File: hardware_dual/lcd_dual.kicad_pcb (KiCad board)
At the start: 2 copper layers, 80 x 50 mm, 128 parts, among them J1 HDMI-A receptacle, J2 USB-C (power + touch USB), J3 AT070TN92 FPC (0.5mm 50P, top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, J4 Touch FPC 6P 0.5mm, J5 SWD/UART, Q1 AO3401A, Q2 2N7002, SW1 BOOT (DFU), SW2 BOOT CH32, U1 LT8619C, U10 STM32F072CBT6 / CH32X035C8T6, U2 AMS1117-3.3, U3 AMS1117-1.8, U4 USBLC6-2SC6, U7 TPS61040, U8 LM321, U9 TPS61165, Y1 25MHz 12pF

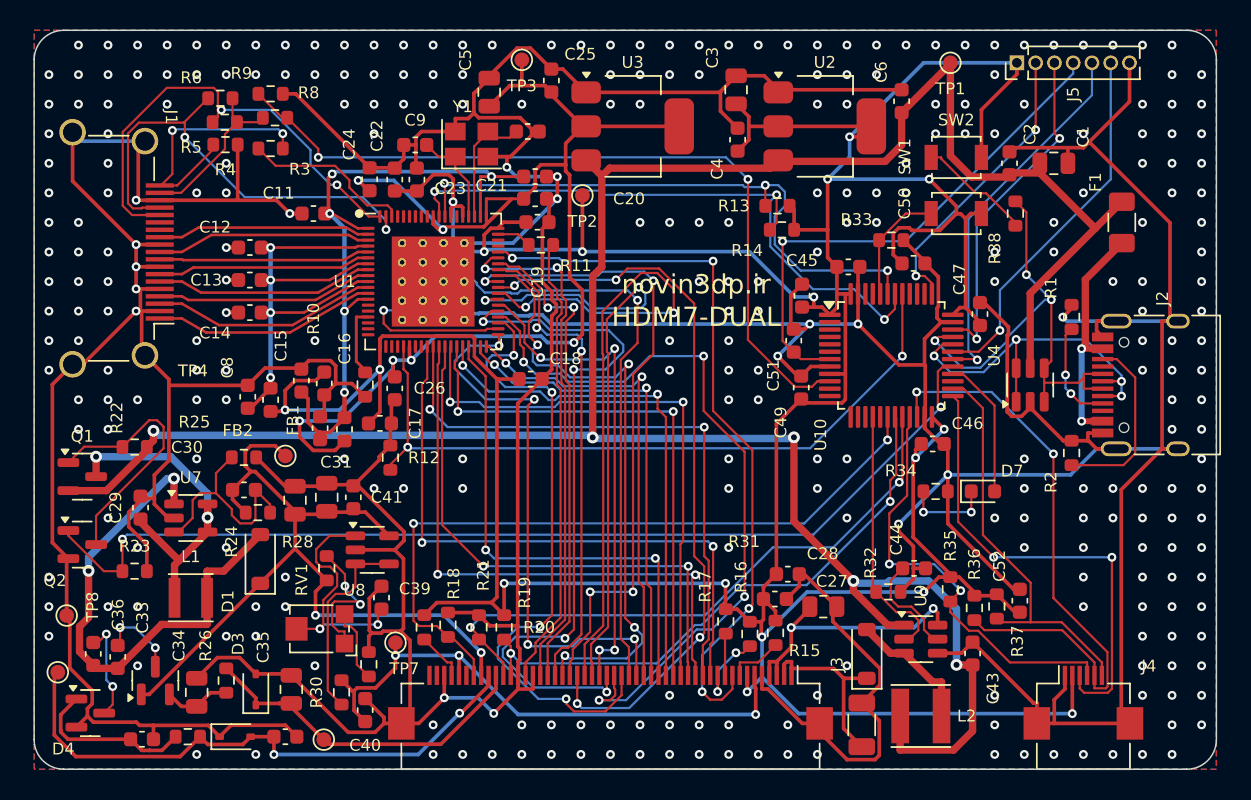
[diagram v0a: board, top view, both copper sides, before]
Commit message: Dual board: aligned passives; firmware: CH32X035 port
PCB (hardware_dual):
- Add a tidy pass after legalize: nearby resistors and capacitors are
  lined up in rows and columns, set to the same orientation and
  snapped to a 0.25 mm grid. A move is kept only if the courtyard
  stays clear (39 parts aligned).
- Rerouted: DRC 0 errors, 0 unconnected, netlist matches design.py.

Firmware:
- Chip-specific code (clock, GPIO, PWM, UART, flash, I2C, USB IRQ)
  now lives behind a small board HAL in src/stm32/ and src/ch32/.
  LT8619C, GT915, USB HID, panel, console and settings logic are
  shared. Both STM32 builds compile without warnings, at the same
  sizes as before.
- New target make BOARD=ch32 for the CH32X035C8T6 on the dual board:
  WCH EVT SDK, TinyUSB master (dcd_ch32_usbfs), bit-banged I2C on both
  buses (with clock stretching and bus recovery), TIM3_CH1 backlight
  PWM, USART1 console, settings in the last 256-byte flash page,
  crystal-less USBFS with the internal D+ pull-up.
  28.9 KB flash, about 4.8 KB RAM; no warnings. Not tested on hardware.
- ./fetch_deps.sh ch32 fetches the SDK and TinyUSB master.

Co-Authored-By: Claude Opus 5.5 <noreply@anthropic.com>
Claude-Session: https://claude.ai/code/session_01X8BrieHZtCS6HfoR48ML9y
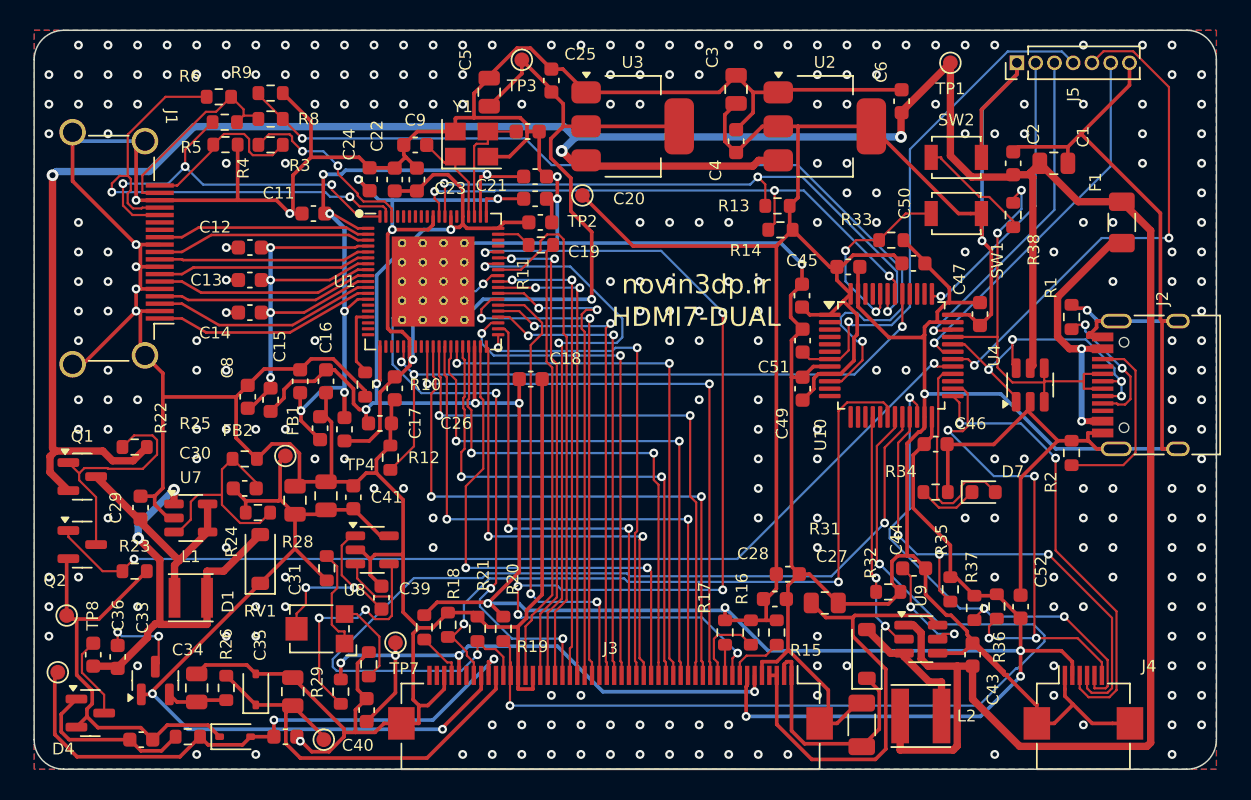
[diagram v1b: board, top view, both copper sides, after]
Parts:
- moved R17 0.75 mm to (146.8, 120.8)
- moved C51 0.60 mm to (152.0, 101.0)
- moved R26 0.50 mm to (113.0, 124.5)
- moved C52 0.40 mm to (166.8, 119.0)
- moved R8 0.31 mm to (116.0, 86.0)
- moved C34 0.30 mm to (111.0, 124.5)
- moved R31 0.27 mm to (153.5, 118.8)
- moved C2 0.25 mm to (166.2, 89.0)
- moved R3 0.25 mm to (116.0, 87.8)
- moved C46 0.20 mm to (161.0, 108.0)
- moved C19 0.19 mm to (134.2, 93.0)
- moved C16 0.19 mm to (119.8, 103.8)
- moved C35 0.18 mm to (117.5, 124.8)
- moved R38 0.18 mm to (166.2, 92.5)
- moved C4 0.14 mm to (147.5, 87.5)
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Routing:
- net +5V: track 173.3 -> 215.8 mm, vias 5 -> 3
- net LCD_LR: track 39.0 -> 67.6 mm
- net GND: track 606.7 -> 580.7 mm, vias 302 -> 268
- net LCD_G4: track 55.0 -> 32.2 mm
- net LCD_UD: track 41.8 -> 64.3 mm
- net LCD_DE: track 49.9 -> 71.0 mm, vias 4 -> 6
- net LCD_G2: track 50.3 -> 31.5 mm, vias 4 -> 2
- net LCD_R5: track 50.1 -> 31.8 mm, vias 4 -> 2
- net LCD_G1: track 48.7 -> 32.1 mm, vias 4 -> 2
- net VLED_K: track 18.4 -> 31.6 mm, vias 2 -> 0
- net LCD_R6: track 46.0 -> 32.8 mm
- net LCD_R4: track 43.5 -> 31.9 mm, vias 4 -> 2
- net UART_TX: track 25.5 -> 35.1 mm, vias 1 -> 2
- net LCD_G3: track 42.7 -> 33.5 mm, vias 4 -> 2
- net HDMI5V_DET: track 53.7 -> 62.5 mm
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
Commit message: Dual board: move the USB-C next to the HDMI receptacle
Same change as on the F042 board: the USB-C sits on the left edge
under the HDMI socket, so both Raspberry Pi cables leave on one side.
The USB pre-routes rotate with the connector, the ESD array moves onto
the USB path, and the bias switch, TPS61040 and fuse are moved to make
room. The logo text moves to the space the USB-C freed on the right.
Routed copper keeps 0.5 mm from the board edge.

Rerouted: DRC 0 errors, 0 unconnected, netlist matches design.py.

Co-Authored-By: Claude Opus 5.5 <noreply@anthropic.com>
Claude-Session: https://claude.ai/code/session_01X8BrieHZtCS6HfoR48ML9y
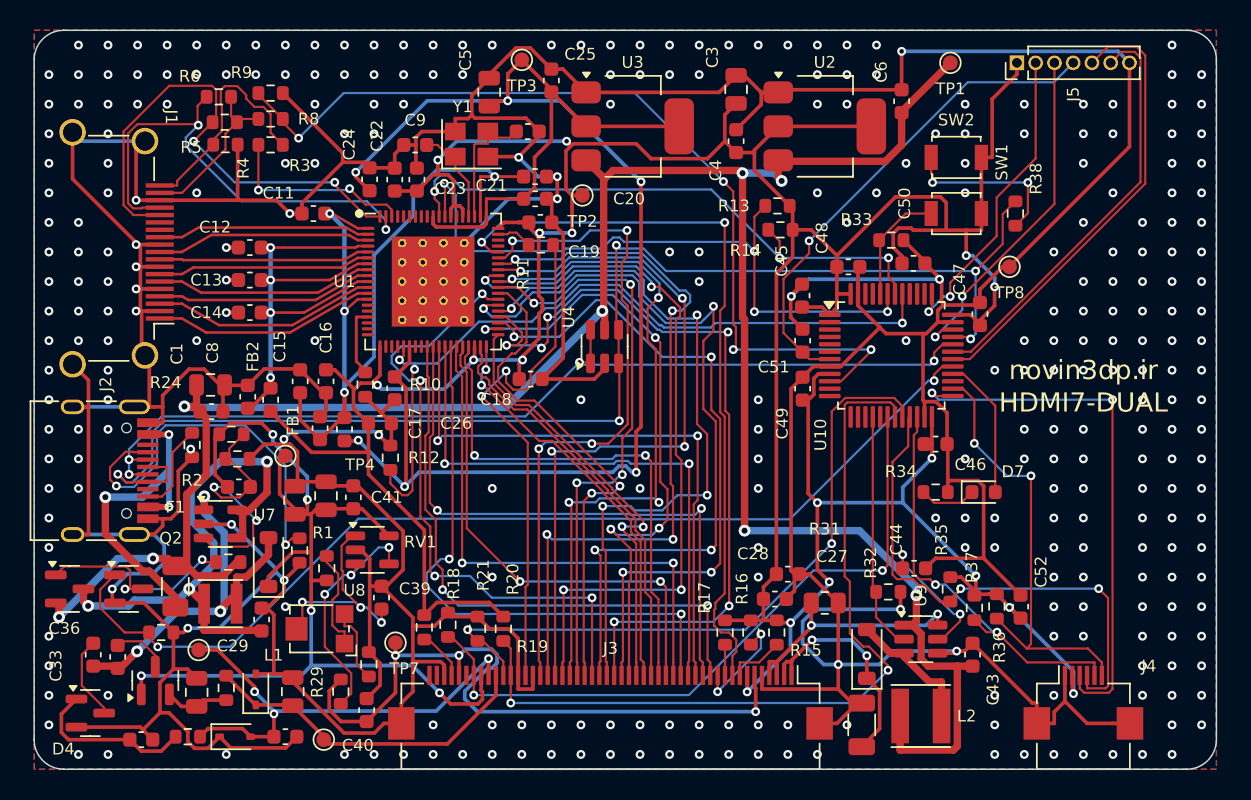
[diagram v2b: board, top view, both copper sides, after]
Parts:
- moved J2 72.9 mm to (103.7, 109.8), turned to -90 degrees
- moved F1 68.6 mm to (109.6, 117.6)
- moved TP8 68.0 mm to (166.0, 96.0)
- moved R2 59.5 mm to (110.7, 108.1), turned to -90 degrees
- moved C1 59.0 mm to (111.9, 104.0)
- moved C2 56.8 mm to (112.0, 105.8), turned to 0 degrees
- moved R1 54.6 mm to (118.0, 115.2), turned to -90 degrees
- moved U4 28.9 mm to (138.6, 101.4)
- moved C29 11.2 mm to (115.4, 119.9)
- moved R22 10.0 mm to (113.1, 116.0)
- moved TP6 9.65 mm to (111.1, 121.9)
- moved Q1 7.65 mm to (102.4, 117.8)
- moved R24 5.60 mm to (113.4, 107.3)
- moved R23 4.52 mm to (108.6, 120.7)
- moved Q2 4.35 mm to (106.4, 117.8)
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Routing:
- net USB_DP: track 28.9 -> 91.7 mm, vias 2 -> 5
- net +5V: track 215.8 -> 161.2 mm, vias 3 -> 8
- net USB_DM: track 23.2 -> 66.5 mm
- net +3V3: track 299.2 -> 272.7 mm, vias 11 -> 17
- net +1V8: track 85.2 -> 110.8 mm, vias 5 -> 6
- net LCD_G0: track 31.9 -> 54.6 mm, vias 2 -> 4
- net LCD_G2: track 31.5 -> 53.2 mm, vias 2 -> 6
- net BOOST_IN: track 15.4 -> 36.3 mm, vias 0 -> 3
- net LCD_DE: track 71.0 -> 50.6 mm, vias 6 -> 2
- net LCD_UD: track 64.3 -> 46.4 mm
- net USB_CC1: track 9.42 -> 26.4 mm
- net LCD_G1: track 32.1 -> 48.3 mm, vias 2 -> 4
- net VLED_K: track 31.6 -> 17.0 mm, vias 0 -> 2
- net LCD_R4: track 31.9 -> 45.7 mm, vias 2 -> 4
- net LCD_LR: track 67.6 -> 54.5 mm
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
